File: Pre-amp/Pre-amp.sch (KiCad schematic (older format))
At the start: 137 parts, among them J1 In, J2 PWR, J3 Send, J4 Return, J5 Out, Q1 J113 NJFET, Q2 J113 NJFET, Q3 J113 NJFET, Q4 J113 NJFET, SW1 Jack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

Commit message: spread out components better.
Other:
- moved on the sheet: C29, C30, C31, C32, D9, R59, R60, R61
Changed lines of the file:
@@
 L Device:R R59
 U 1 1 5CDABE09
-P 10950 6650
-F 0 "R59" V 10743 6650 50  0000 C CNN
-F 1 "3.3k" V 10834 6650 50  0000 C CNN
-F 2 "Resistors_THT:R_Axial_DIN0204_L3.6mm_D1.6mm_P5.08mm_Horizontal" V 10880 6650 50  0001 C CNN
-F 3 "~" H 10950 6650 50  0001 C CNN
-	1    10950 6650
+P 10750 6650
+F 0 "R59" V 10543 6650 50  0000 C CNN
+F 1 "3.3k" V 10634 6650 50  0000 C CNN
+F 2 "Resistors_THT:R_Axial_DIN0204_L3.6mm_D1.6mm_P5.08mm_Horizontal" V 10680 6650 50  0001 C CNN
+F 3 "~" H 10750 6650 50  0001 C CNN
+	1    10750 6650
 	0    1    1    0
 $EndComp
@@
 L Device:R R60
 U 1 1 5CDAC229
-P 10950 7900
-F 0 "R60" V 10743 7900 50  0000 C CNN
-F 1 "3.3k" V 10834 7900 50  0000 C CNN
-F 2 "Resistors_THT:R_Axial_DIN0204_L3.6mm_D1.6mm_P5.08mm_Horizontal" V 10880 7900 50  0001 C CNN
-F 3 "~" H 10950 7900 50  0001 C CNN
-	1    10950 7900
+P 10750 7900
+F 0 "R60" V 10543 7900 50  0000 C CNN
+F 1 "3.3k" V 10634 7900 50  0000 C CNN
+F 2 "Resistors_THT:R_Axial_DIN0204_L3.6mm_D1.6mm_P5.08mm_Horizontal" V 10680 7900 50  0001 C CNN
+F 3 "~" H 10750 7900 50  0001 C CNN
+	1    10750 7900
 	0    1    1    0
 $EndComp
@@
 L Device:CP C31
 U 1 1 5CDAC3E8
-P 11450 6900
-F 0 "C31" H 11600 6800 50  0000 C CNN
-F 1 "10uf" H 11600 7000 50  0000 C CNN
-F 2 "Capacitor_THT:CP_Radial_D4.0mm_P1.50mm" H 11488 6750 50  0001 C CNN
-F 3 "~" H 11450 6900 50  0001 C CNN
-	1    11450 6900
+P 11250 6900
+F 0 "C31" H 11400 6800 50  0000 C CNN
+F 1 "10uf" H 11400 7000 50  0000 C CNN
+F 2 "Capacitor_THT:CP_Radial_D4.0mm_P1.50mm" H 11288 6750 50  0001 C CNN
+F 3 "~" H 11250 6900 50  0001 C CNN
+	1    11250 6900
 	1    0    0    -1
 $EndComp
@@
 L Device:CP C32
 U 1 1 5CDACA0C
-P 11450 7600
-F 0 "C32" H 11600 7450 50  0000 C CNN
-F 1 "10uf" H 11600 7750 50  0000 C CNN
-F 2 "Capacitor_THT:CP_Radial_D4.0mm_P1.50mm" H 11488 7450 50  0001 C CNN
-F 3 "~" H 11450 7600 50  0001 C CNN
-	1    11450 7600
+P 11250 7600
+F 0 "C32" H 11400 7450 50  0000 C CNN
+F 1 "10uf" H 11400 7750 50  0000 C CNN
+F 2 "Capacitor_THT:CP_Radial_D4.0mm_P1.50mm" H 11288 7450 50  0001 C CNN
+F 3 "~" H 11250 7600 50  0001 C CNN
+	1    11250 7600
 	1    0    0    -1
 $EndComp
@@
 L Device:C C29
 U 1 1 5CDAD6B5
-P 10450 6900
-F 0 "C29" H 10650 6800 50  0000 C CNN
-F 1 "0.01uf" H 10600 7000 50  0000 C CNN
-F 2 "Capacitor_THT:C_Disc_D3.8mm_W2.6mm_P2.50mm" H 10488 6750 50  0001 C CNN
-F 3 "~" H 10450 6900 50  0001 C CNN
-	1    10450 6900
+P 10250 6900
+F 0 "C29" H 10450 6800 50  0000 C CNN
+F 1 "0.01uf" H 10400 7000 50  0000 C CNN
+F 2 "Capacitor_THT:C_Disc_D3.8mm_W2.6mm_P2.50mm" H 10288 6750 50  0001 C CNN
+F 3 "~" H 10250 6900 50  0001 C CNN
+	1    10250 6900
 	1    0    0    -1
 $EndComp
@@
 L Device:C C30
 U 1 1 5CDADB14
-P 10450 7600
-F 0 "C30" H 10650 7500 50  0000 C CNN
-F 1 "0.01uf" H 10600 7700 50  0000 C CNN
-F 2 "Capacitor_THT:C_Disc_D3.8mm_W2.6mm_P2.50mm" H 10488 7450 50  0001 C CNN
-F 3 "~" H 10450 7600 50  0001 C CNN
-	1    10450 7600
+P 10250 7600
+F 0 "C30" H 10450 7500 50  0000 C CNN
+F 1 "0.01uf" H 10400 7700 50  0000 C CNN
+F 2 "Capacitor_THT:C_Disc_D3.8mm_W2.6mm_P2.50mm" H 10288 7450 50  0001 C CNN
+F 3 "~" H 10250 7600 50  0001 C CNN
+	1    10250 7600
 	1    0    0    -1
 $EndComp
@@
 L Device:R R61
 U 1 1 5CE0A934
-P 10950 8250
-F 0 "R61" V 10743 8250 50  0000 C CNN
-F 1 "1k" V 10834 8250 50  0000 C CNN
-F 2 "Resistors_THT:R_Axial_DIN0204_L3.6mm_D1.6mm_P5.08mm_Horizontal" V 10880 8250 50  0001 C CNN
-F 3 "~" H 10950 8250 50  0001 C CNN
-	1    10950 8250
-	0    1    1    0
-$EndComp
-Wire Wire Line
-	10450 6750 10450 6650
-Wire Wire Line
-	10450 6650 10800 6650
-Wire Wire Line
-	11100 6650 11450 6650
-Wire Wire Line
-	11450 6650 11450 6750
-Wire Wire Line
-	11450 7050 11450 7250
-Wire Wire Line
-	10450 7050 10450 7250
-Wire Wire Line
-	10450 7750 10450 7900
-Wire Wire Line
-	10450 7900 10800 7900
-Wire Wire Line
-	11100 7900 11450 7900
-Wire Wire Line
-	11450 7900 11450 7750
-Wire Wire Line
-	10800 8250 10450 8250
-Wire Wire Line
-	10450 8250 10450 7900
-Connection ~ 10450 7900
-Wire Wire Line
-	10450 7250 11450 7250
-Connection ~ 10450 7250
-Wire Wire Line
-	10450 7250 10450 7450
-Connection ~ 11450 7250
-Wire Wire Line
-	11450 7250 11450 7450
+P 10750 8250
+F 0 "R61" V 10543 8250 50  0000 C CNN
+F 1 "1k" V 10634 8250 50  0000 C CNN
+F 2 "Resistors_THT:R_Axial_DIN0204_L3.6mm_D1.6mm_P5.08mm_Horizontal" V 10680 8250 50  0001 C CNN
+F 3 "~" H 10750 8250 50  0001 C CNN
+	1    10750 8250
+	0    1    1    0
+$EndComp
+Wire Wire Line
+	10250 6750 10250 6650
+Wire Wire Line
+	10250 6650 10600 6650
+Wire Wire Line
+	10900 6650 11250 6650
+Wire Wire Line
+	11250 6650 11250 6750
+Wire Wire Line
+	11250 7050 11250 7250
+Wire Wire Line
+	10250 7050 10250 7250
+Wire Wire Line
+	10250 7750 10250 7900
+Wire Wire Line
+	10250 7900 10600 7900
+Wire Wire Line
+	10900 7900 11250 7900
+Wire Wire Line
+	11250 7900 11250 7750
+Wire Wire Line
+	10600 8250 10250 8250
+Wire Wire Line
+	10250 8250 10250 7900
+Connection ~ 10250 7900
+Wire Wire Line
+	10250 7250 11250 7250
+Connection ~ 10250 7250
+Wire Wire Line
+	10250 7250 10250 7450
+Connection ~ 11250 7250
+Wire Wire Line
+	11250 7250 11250 7450
 $Comp
 L power:GND #PWR033
 U 1 1 5CF82DD3
-P 11950 7300
-F 0 "#PWR033" H 11950 7050 50  0001 C CNN
-F 1 "GND" H 11955 7127 50  0000 C CNN
-F 2 "" H 11950 7300 50  0001 C CNN
-F 3 "" H 11950 7300 50  0001 C CNN
-	1    11950 7300
-	1    0    0    -1
-$EndComp
-Wire Wire Line
-	11450 7250 11950 7250
-Wire Wire Line
-	11950 7250 11950 7300
+P 11750 7300
+F 0 "#PWR033" H 11750 7050 50  0001 C CNN
+F 1 "GND" H 11755 7127 50  0000 C CNN
+F 2 "" H 11750 7300 50  0001 C CNN
+F 3 "" H 11750 7300 50  0001 C CNN
+	1    11750 7300
+	1    0    0    -1
+$EndComp
+Wire Wire Line
+	11250 7250 11750 7250
+Wire Wire Line
+	11750 7250 11750 7300
 $Comp
 L Device:D D9
 U 1 1 5CFB3B2A
-P 11450 8250
-F 0 "D9" H 11450 8466 50  0000 C CNN
-F 1 "1N4002" H 11450 8375 50  0000 C CNN
-F 2 "Diode_THT:D_DO-41_SOD81_P7.62mm_Horizontal" H 11450 8250 50  0001 C CNN
-F 3 "~" H 11450 8250 50  0001 C CNN
-	1    11450 8250
-	1    0    0    -1
-$EndComp
-Wire Wire Line
-	11300 8250 11100 8250
+P 11250 8250
+F 0 "D9" H 11250 8466 50  0000 C CNN
+F 1 "1N4002" H 11250 8375 50  0000 C CNN
+F 2 "Diode_THT:D_DO-41_SOD81_P7.62mm_Horizontal" H 11250 8250 50  0001 C CNN
+F 3 "~" H 11250 8250 50  0001 C CNN
+	1    11250 8250
+	1    0    0    -1
+$EndComp
+Wire Wire Line
+	11100 8250 10900 8250
 $Comp
 L power:GND #PWR032
 U 1 1 5D018DF0
-P 11900 8400
-F 0 "#PWR032" H 11900 8150 50  0001 C CNN
-F 1 "GND" H 11905 8227 50  0000 C CNN
-F 2 "" H 11900 8400 50  0001 C CNN
-F 3 "" H 11900 8400 50  0001 C CNN
-	1    11900 8400
-	1    0    0    -1
-$EndComp
-Wire Wire Line
-	11600 8250 11900 8250
-Wire Wire Line
-	11900 8250 11900 8400
-Wire Wire Line
-	11450 7900 11700 7900
-Connection ~ 11450 7900
-Text GLabel 11700 7900 2    50   Input ~ 0
+P 11700 8400
+F 0 "#PWR032" H 11700 8150 50  0001 C CNN
+F 1 "GND" H 11705 8227 50  0000 C CNN
+F 2 "" H 11700 8400 50  0001 C CNN
+F 3 "" H 11700 8400 50  0001 C CNN
+	1    11700 8400
+	1    0    0    -1
+$EndComp
+Wire Wire Line
+	11400 8250 11700 8250
+Wire Wire Line
+	11700 8250 11700 8400
+Wire Wire Line
+	11250 7900 11500 7900
+Connection ~ 11250 7900
+Text GLabel 11500 7900 2    50   Input ~ 0
 E
 Wire Wire Line
-	10450 6650 10250 6650
-Connection ~ 10450 6650
-Wire Wire Line
-	11450 6650 11750 6650
-Connection ~ 11450 6650
-Text GLabel 11750 6650 2    50   Input ~ 0
+	10250 6650 10050 6650
+Connection ~ 10250 6650
+Wire Wire Line
+	11250 6650 11550 6650
+Connection ~ 11250 6650
+Text GLabel 11550 6650 2    50   Input ~ 0
 D
-Text GLabel 10250 6650 0    50   Input ~ 0
+Text GLabel 10050 6650 0    50   Input ~ 0
 B
 Wire Wire Line
-	10450 7900 10200 7900
-Text GLabel 10200 7900 0    50   Input ~ 0
+	10250 7900 10000 7900
+Text GLabel 10000 7900 0    50   Input ~ 0
 C
 $Comp
@@
 Wire Wire Line
 	5100 500  7750 500
-$Comp
-L Analog_Switch:DG419LDJ U6
-U 2 1 5EBF0578
-P 5650 3700
-F 0 "U6" H 5650 3942 50  0000 C CNN
-F 1 "DG419LDJ" H 5650 3851 50  0000 C CNN
-F 2 "Package_DIP:DIP-8_W7.62mm_LongPads" H 5650 3400 50  0001 C CNN
-F 3 "https://datasheets.maximintegrated.com/en/ds/DG417-DG419.pdf" H 5650 3500 50  0001 C CNN
-	2    5650 3700
-	0    1    1    0
-$EndComp
 Text GLabel 6850 700  0    50   Input ~ 0
 CLEAN-IN
@@
 	1    0    0    -1
 $EndComp
+$Comp
+L Analog_Switch:DG419LDJ U6
+U 2 1 5EBF0578
+P 5650 3700
+F 0 "U6" V 5450 3700 50  0000 C CNN
+F 1 "DG419LDJ" V 6000 3700 50  0000 C CNN
+F 2 "Package_DIP:DIP-8_W7.62mm_LongPads" H 5650 3400 50  0001 C CNN
+F 3 "https://datasheets.maximintegrated.com/en/ds/DG417-DG419.pdf" H 5650 3500 50  0001 C CNN
+	2    5650 3700
+	0    1    1    0
+$EndComp
 $EndSCHEMATC

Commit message: tweak PCB layout
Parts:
- D10: footprint LEDs:LED_D3.0mm -> Connector_PinHeader_2.00mm:PinHeader_2x01_P2.00mm_Vertical
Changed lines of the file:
@@
 F 0 "D10" H 1393 4516 50  0000 C CNN
 F 1 "LED" H 1393 4425 50  0000 C CNN
-F 2 "LEDs:LED_D3.0mm" H 1400 4300 50  0001 C CNN
+F 2 "Connector_PinHeader_2.00mm:PinHeader_2x01_P2.00mm_Vertical" H 1400 4300 50  0001 C CNN
 F 3 "~" H 1400 4300 50  0001 C CNN
 	1    1400 4300

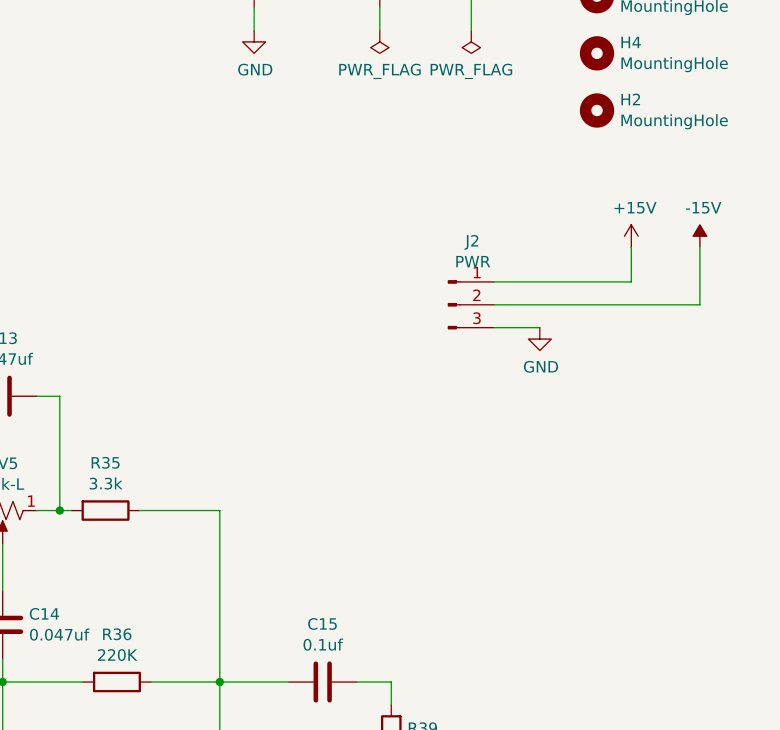
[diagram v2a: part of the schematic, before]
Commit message: add power caps
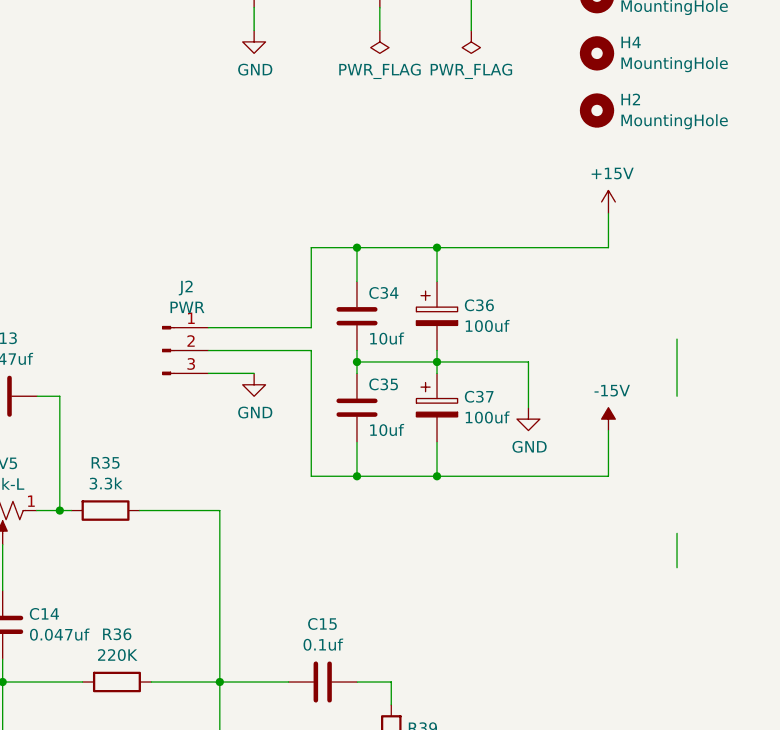
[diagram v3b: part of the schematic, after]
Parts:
- added C34, C35: 10uf, Capacitor_THT:C_Disc_D6.0mm_W2.5mm_P5.00mm, symbol Device:C
- added C36, C37: 100uf, Capacitor_THT:CP_Radial_D8.0mm_P5.00mm, symbol Device:CP
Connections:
- net +15V: now also C34.1, C36.1
- net -15V: now also C35.2, C37.2
- net GND: now also C34.2, C35.1, C36.2, C37.1
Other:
- moved on the sheet: J2
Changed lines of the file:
@@
 L Connector:Conn_01x03_Male J2
 U 1 1 5C81D105
-P 15100 2200
-F 0 "J2" H 15206 2478 50  0000 C CNN
-F 1 "PWR" H 15206 2387 50  0000 C CNN
-F 2 "Connector_PinHeader_2.00mm:PinHeader_1x03_P2.00mm_Vertical" H 15100 2200 50  0001 C CNN
-F 3 "~" H 15100 2200 50  0001 C CNN
-	1    15100 2200
+P 13850 2400
+F 0 "J2" H 13956 2678 50  0000 C CNN
+F 1 "PWR" H 13956 2587 50  0000 C CNN
+F 2 "Connector_PinHeader_2.00mm:PinHeader_1x03_P2.00mm_Vertical" H 13850 2400 50  0001 C CNN
+F 3 "~" H 13850 2400 50  0001 C CNN
+	1    13850 2400
 	1    0    0    -1
 $EndComp
@@
 L power:GND #PWR09
 U 1 1 5C8243F7
-P 15500 2300
-F 0 "#PWR09" H 15500 2050 50  0001 C CNN
-F 1 "GND" H 15505 2127 50  0000 C CNN
-F 2 "" H 15500 2300 50  0001 C CNN
-F 3 "" H 15500 2300 50  0001 C CNN
-	1    15500 2300
+P 14250 2500
+F 0 "#PWR09" H 14250 2250 50  0001 C CNN
+F 1 "GND" H 14255 2327 50  0000 C CNN
+F 2 "" H 14250 2500 50  0001 C CNN
+F 3 "" H 14250 2500 50  0001 C CNN
+	1    14250 2500
 	1    0    0    -1
 $EndComp
@@
 L power:+15V #PWR010
 U 1 1 5C824A10
-P 15900 1950
-F 0 "#PWR010" H 15900 1800 50  0001 C CNN
-F 1 "+15V" H 15915 2123 50  0000 C CNN
-F 2 "" H 15900 1950 50  0001 C CNN
-F 3 "" H 15900 1950 50  0001 C CNN
-	1    15900 1950
+P 15800 1800
+F 0 "#PWR010" H 15800 1650 50  0001 C CNN
+F 1 "+15V" H 15815 1973 50  0000 C CNN
+F 2 "" H 15800 1800 50  0001 C CNN
+F 3 "" H 15800 1800 50  0001 C CNN
+	1    15800 1800
 	1    0    0    -1
 $EndComp
@@
 L power:-15V #PWR011
 U 1 1 5C825029
-P 16200 1950
-F 0 "#PWR011" H 16200 2050 50  0001 C CNN
-F 1 "-15V" H 16215 2123 50  0000 C CNN
-F 2 "" H 16200 1950 50  0001 C CNN
-F 3 "" H 16200 1950 50  0001 C CNN
-	1    16200 1950
-	1    0    0    -1
-$EndComp
-Wire Wire Line
-	15300 2100 15900 2100
-Wire Wire Line
-	15900 2100 15900 1950
-Wire Wire Line
-	15300 2200 16200 2200
-Wire Wire Line
-	16200 2200 16200 1950
-Wire Wire Line
-	15300 2300 15500 2300
+P 15800 2750
+F 0 "#PWR011" H 15800 2850 50  0001 C CNN
+F 1 "-15V" H 15815 2923 50  0000 C CNN
+F 2 "" H 15800 2750 50  0001 C CNN
+F 3 "" H 15800 2750 50  0001 C CNN
+	1    15800 2750
+	1    0    0    -1
+$EndComp
+Wire Wire Line
+	14050 2300 14500 2300
+Wire Wire Line
+	16100 3350 16100 3200
+Wire Wire Line
+	14050 2400 14500 2400
+Wire Wire Line
+	16100 2600 16100 2350
+Wire Wire Line
+	14050 2500 14250 2500
 $Comp
 L Mechanical:MountingHole H2
@@
 	0    1    1    0
 $EndComp
+$Comp
+L Device:CP C36
+U 1 1 5CDC1AC0
+P 15050 2250
+F 0 "C36" H 15168 2296 50  0000 L CNN
+F 1 "100uf" H 15168 2205 50  0000 L CNN
+F 2 "Capacitor_THT:CP_Radial_D8.0mm_P5.00mm" H 15088 2100 50  0001 C CNN
+F 3 "~" H 15050 2250 50  0001 C CNN
+	1    15050 2250
+	1    0    0    -1
+$EndComp
+$Comp
+L Device:CP C37
+U 1 1 5CDC21FA
+P 15050 2650
+F 0 "C37" H 15168 2696 50  0000 L CNN
+F 1 "100uf" H 15168 2605 50  0000 L CNN
+F 2 "Capacitor_THT:CP_Radial_D8.0mm_P5.00mm" H 15088 2500 50  0001 C CNN
+F 3 "~" H 15050 2650 50  0001 C CNN
+	1    15050 2650
+	1    0    0    -1
+$EndComp
+$Comp
+L Device:C C34
+U 1 1 5CDC35F9
+P 14700 2250
+F 0 "C34" H 14750 2350 50  0000 L CNN
+F 1 "10uf" H 14750 2150 50  0000 L CNN
+F 2 "Capacitor_THT:C_Disc_D6.0mm_W2.5mm_P5.00mm" H 14738 2100 50  0001 C CNN
+F 3 "~" H 14700 2250 50  0001 C CNN
+	1    14700 2250
+	1    0    0    -1
+$EndComp
+$Comp
+L Device:C C35
+U 1 1 5CDC3E5A
+P 14700 2650
+F 0 "C35" H 14750 2750 50  0000 L CNN
+F 1 "10uf" H 14750 2550 50  0000 L CNN
+F 2 "Capacitor_THT:C_Disc_D6.0mm_W2.5mm_P5.00mm" H 14738 2500 50  0001 C CNN
+F 3 "~" H 14700 2650 50  0001 C CNN
+	1    14700 2650
+	1    0    0    -1
+$EndComp
+Wire Wire Line
+	14700 2500 14700 2450
+Wire Wire Line
+	15050 2500 15050 2450
+Wire Wire Line
+	14500 2950 14700 2950
+Wire Wire Line
+	14700 2950 14700 2800
+Wire Wire Line
+	14500 2400 14500 2950
+Wire Wire Line
+	15050 2800 15050 2950
+Wire Wire Line
+	15050 2950 14700 2950
+Connection ~ 14700 2950
+Wire Wire Line
+	14700 2450 15050 2450
+Connection ~ 14700 2450
+Wire Wire Line
+	14700 2450 14700 2400
+Connection ~ 15050 2450
+Wire Wire Line
+	15050 2450 15050 2400
+Wire Wire Line
+	15050 2450 15450 2450
+Wire Wire Line
+	15450 2450 15450 2650
+$Comp
+L power:GND #PWR042
+U 1 1 5D0B329C
+P 15450 2650
+F 0 "#PWR042" H 15450 2400 50  0001 C CNN
+F 1 "GND" H 15455 2477 50  0000 C CNN
+F 2 "" H 15450 2650 50  0001 C CNN
+F 3 "" H 15450 2650 50  0001 C CNN
+	1    15450 2650
+	1    0    0    -1
+$EndComp
+Wire Wire Line
+	14500 2300 14500 1950
+Wire Wire Line
+	14500 1950 14700 1950
+Wire Wire Line
+	14700 1950 14700 2100
+Wire Wire Line
+	15050 2100 15050 1950
+Wire Wire Line
+	15050 1950 14700 1950
+Connection ~ 14700 1950
+Wire Wire Line
+	15050 2950 15800 2950
+Wire Wire Line
+	15800 2950 15800 2750
+Connection ~ 15050 2950
+Wire Wire Line
+	15050 1950 15800 1950
+Wire Wire Line
+	15800 1950 15800 1800
+Connection ~ 15050 1950
 $EndSCHEMATC

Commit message: fix 1uf caps to CP
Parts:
- C18, C22, C23, C25: footprint Capacitor_THT:C_Disc_D3.8mm_W2.6mm_P2.50mm -> Capacitor_THT:CP_Radial_D4.0mm_P1.50mm
- C33: footprint Capacitors_THT:C_Disc_D3.8mm_W2.6mm_P2.50mm -> Capacitor_THT:C_Rect_L7.0mm_W2.0mm_P5.00mm
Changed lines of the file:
@@
 F 0 "C18" H 4218 8146 50  0000 L CNN
 F 1 "1uf" H 4218 8055 50  0000 L CNN
-F 2 "Capacitor_THT:C_Disc_D3.8mm_W2.6mm_P2.50mm" H 4138 7950 50  0001 C CNN
+F 2 "Capacitor_THT:CP_Radial_D4.0mm_P1.50mm" H 4138 7950 50  0001 C CNN
 F 3 "~" H 4100 8100 50  0001 C CNN
 	1    4100 8100
@@
 F 0 "C23" H 7168 9396 50  0000 L CNN
 F 1 "1uf" H 7168 9305 50  0000 L CNN
-F 2 "Capacitor_THT:C_Disc_D3.8mm_W2.6mm_P2.50mm" H 7088 9200 50  0001 C CNN
+F 2 "Capacitor_THT:CP_Radial_D4.0mm_P1.50mm" H 7088 9200 50  0001 C CNN
 F 3 "~" H 7050 9350 50  0001 C CNN
 	1    7050 9350
@@
 F 0 "C22" V 5350 6400 50  0000 C CNN
 F 1 "1uf" V 5700 6400 50  0000 C CNN
-F 2 "Capacitor_THT:C_Disc_D3.8mm_W2.6mm_P2.50mm" H 5538 6250 50  0001 C CNN
+F 2 "Capacitor_THT:CP_Radial_D4.0mm_P1.50mm" H 5538 6250 50  0001 C CNN
 F 3 "~" H 5500 6400 50  0001 C CNN
 	1    5500 6400
@@
 F 0 "C25" V 8295 8000 50  0000 C CNN
 F 1 "1uf" V 8386 8000 50  0000 C CNN
-F 2 "Capacitor_THT:C_Disc_D3.8mm_W2.6mm_P2.50mm" H 8588 7850 50  0001 C CNN
+F 2 "Capacitor_THT:CP_Radial_D4.0mm_P1.50mm" H 8588 7850 50  0001 C CNN
 F 3 "~" H 8550 8000 50  0001 C CNN
 	1    8550 8000
@@
 F 0 "C33" H 3915 5396 50  0000 L CNN
 F 1 "1uF" H 3915 5305 50  0000 L CNN
-F 2 "Capacitors_THT:C_Disc_D3.8mm_W2.6mm_P2.50mm" H 3838 5200 50  0001 C CNN
+F 2 "Capacitor_THT:C_Rect_L7.0mm_W2.0mm_P5.00mm" H 3838 5200 50  0001 C CNN
 F 3 "~" H 3800 5350 50  0001 C CNN
 	1    3800 5350
